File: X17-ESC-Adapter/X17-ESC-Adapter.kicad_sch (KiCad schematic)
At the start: 9 parts, among them J2 Power In/Out

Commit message: 10/12/24
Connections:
- net ESC2B: now also ESC5.5 (M2P2); no longer ESC5.6 (M2P3)
- net ESC2C: now also ESC5.6 (M2P3); no longer ESC5.5 (M2P2)

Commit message: before design review
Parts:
- added J1: Pad for ESC, Connector_Wire:SolderWirePad_1x01_SMD_1x2mm, symbol Connector:Conn_01x01_Pin
- J2: value Power In/Out -> PWM JST Connector
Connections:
- net +5V: now reaches BM08B-SRSS-TBLFSN1.1
- net +5V: now also J2.05
- net Current ADC: now reaches BM08B-SRSS-TBLFSN1.3
- net Current ADC: now also J2.07
- net Telemetry: now reaches BM08B-SRSS-TBLFSN1.4
- net Telemetry: now also J2.09
- net MTR_1 renamed PWM1
- net MTR_2 renamed PWM2
- net MTR_3 renamed PWM3
- net MTR_4 renamed PWM4
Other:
- moved on the sheet: ESC1, ESC2, ESC3, ESC4, ESC5

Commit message: made some changes
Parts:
- added J10, J11, J12, J13, J3, J4, J5, J6, J7, J8, J9: Pad for ESC, Custom ROV Parts:Pad for ESC Adapter, symbol Connector:Conn_01x01_Pin
- J1: footprint Connector_Wire:SolderWirePad_1x01_SMD_1x2mm -> Custom ROV Parts:Pad for ESC Adapter
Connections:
- net +5V: now also J2.09; no longer J2.05
- net ESC1A: now also ESC1.5, ESC1.6, J4.1 (Pin_1); no longer ESC1.1, ESC1.2
- net ESC1B: now also J3.1 (Pin_1)
- net ESC1C: now also ESC1.1, ESC1.2, J1.1 (Pin_1); no longer ESC1.5, ESC1.6
- net ESC2A: now also ESC2.5, ESC2.6, J7.1 (Pin_1); no longer ESC2.1, ESC2.2
- net ESC2B: now also J6.1 (Pin_1)
- net ESC2C: now also ESC2.1, ESC2.2, J5.1 (Pin_1); no longer ESC2.5, ESC2.6
- net ESC3A: now also J8.1 (Pin_1)
- net ESC3B: now also J10.1 (Pin_1)
- net ESC3C: now also J9.1 (Pin_1)
- net ESC4A: now also J11.1 (Pin_1)
- net ESC4B: now also J12.1 (Pin_1)
- net ESC4C: now also J13.1 (Pin_1)
- net PWM1: now also J2.10; no longer J2.04
- net PWM2: now also J2.08; no longer J2.06
- net PWM3: now also J2.06; no longer J2.08
- net PWM4: now also J2.04; no longer J2.10
- net Telemetry: now also J2.05; no longer J2.09
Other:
- note added: "Connection to Thrusters"
- note added: "Lumenier ESC"
- note added: "Power Testing LED"

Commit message: final before alumni design review
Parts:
- J1, J10, J11, J12, J13, J3, J4, J5, J6, J7, J8, J9: footprint Custom ROV Parts:Pad for ESC Adapter -> pad for esc connectors:Pad for ESC Adapter
- J2: value PWM JST Connector -> PWM Connector
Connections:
- net +12V: no longer J2.01
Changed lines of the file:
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@@
 	(wire
 		(pts
-			(xy 115.57 115.57) (xy 107.95 115.57)
-		)
-		(stroke
-			(width 0)
-			(type default)
-		)
-	)
-	(wire
-		(pts
 			(xy 135.89 95.25) (xy 143.51 95.25)
 		)
@@
 	(wire
 		(pts
-			(xy 81.28 96.52) (xy 81.28 92.71)
+			(xy 102.87 99.06) (xy 102.87 95.25)
 		)
 		(stroke
@@
 	(wire
 		(pts
-			(xy 67.31 96.52) (xy 67.31 92.71)
+			(xy 92.71 99.06) (xy 92.71 95.25)
 		)
 		(stroke
@@
 	(wire
 		(pts
-			(xy 97.79 96.52) (xy 97.79 92.71)
+			(xy 113.03 99.06) (xy 113.03 95.25)
 		)
 		(stroke
@@
 	(symbol
 		(lib_id "power:GND")
-		(at 81.28 96.52 0)
+		(at 102.87 99.06 0)
 		(unit 1)
 		(exclude_from_sim no)
@@
 		(fields_autoplaced yes)
 		(property "Reference" "#PWR012"
-			(at 81.28 102.87 0)
+			(at 102.87 105.41 0)
 			(effects
 				(font
@@
 		)
 		(property "Value" "GND"
-			(at 81.28 101.6 0)
+			(at 102.87 104.14 0)
 			(effects
 				(font
@@
 		)
 		(property "Footprint" ""
-			(at 81.28 96.52 0)
+			(at 102.87 99.06 0)
 			(effects
 				(font
@@
 		)
 		(property "Datasheet" ""
-			(at 81.28 96.52 0)
+			(at 102.87 99.06 0)
 			(effects
 				(font
@@
 		)
 		(property "Description" "Power symbol creates a global label with name \"GND\" , ground"
-			(at 81.28 96.52 0)
+			(at 102.87 99.06 0)
 			(effects
 				(font
@@
 	(symbol
 		(lib_id "power:PWR_FLAG")
-		(at 97.79 92.71 0)
+		(at 113.03 95.25 0)
 		(unit 1)
 		(exclude_from_sim no)
@@
 		(fields_autoplaced yes)
 		(property "Reference" "#FLG01"
-			(at 97.79 90.805 0)
+			(at 113.03 93.345 0)
 			(effects
 				(font
@@
 		)
 		(property "Value" "PWR_FLAG"
-			(at 97.79 87.63 0)
+			(at 113.03 90.17 0)
 			(effects
 				(font
@@
 		)
 		(property "Footprint" ""
-			(at 97.79 92.71 0)
+			(at 113.03 95.25 0)
 			(effects
 				(font
@@
 		)
 		(property "Datasheet" "~"
-			(at 97.79 92.71 0)
+			(at 113.03 95.25 0)
 			(effects
 				(font
@@
 		)
 		(property "Description" "Special symbol for telling ERC where power comes from"
-			(at 97.79 92.71 0)
+			(at 113.03 95.25 0)
 			(effects
 				(font
@@
 			)
 		)
-		(property "Footprint" "Custom ROV Parts:Pad for ESC Adapter"
+		(property "Footprint" "pad for esc connectors:Pad for ESC Adapter"
 			(at 219.71 102.87 0)
 			(effects
@@
 			)
 		)
-		(property "Footprint" "Custom ROV Parts:Pad for ESC Adapter"
+		(property "Footprint" "pad for esc connectors:Pad for ESC Adapter"
 			(at 220.98 111.76 0)
 			(effects
@@
 	(symbol
 		(lib_id "power:PWR_FLAG")
-		(at 67.31 92.71 0)
+		(at 92.71 95.25 0)
 		(unit 1)
 		(exclude_from_sim no)
@@
 		(fields_autoplaced yes)
 		(property "Reference" "#FLG03"
-			(at 67.31 90.805 0)
+			(at 92.71 93.345 0)
 			(effects
 				(font
@@
 		)
 		(property "Value" "PWR_FLAG"
-			(at 67.31 87.63 0)
+			(at 92.71 90.17 0)
 			(effects
 				(font
@@
 		)
 		(property "Footprint" ""
-			(at 67.31 92.71 0)
+			(at 92.71 95.25 0)
 			(effects
 				(font
@@
 		)
 		(property "Datasheet" "~"
-			(at 67.31 92.71 0)
+			(at 92.71 95.25 0)
 			(effects
 				(font
@@
 		)
 		(property "Description" "Special symbol for telling ERC where power comes from"
-			(at 67.31 92.71 0)
+			(at 92.71 95.25 0)
 			(effects
 				(font
@@
 	)
 	(symbol
-		(lib_id "power:+12V")
-		(at 107.95 115.57 90)
-		(unit 1)
-		(exclude_from_sim no)
-		(in_bom yes)
-		(on_board yes)
-		(dnp no)
-		(fields_autoplaced yes)
-		(property "Reference" "#PWR03"
-			(at 111.76 115.57 0)
-			(effects
-				(font
-					(size 1.27 1.27)
-				)
-				(hide yes)
-			)
-		)
-		(property "Value" "+12V"
-			(at 104.14 115.5699 90)
-			(effects
-				(font
-					(size 1.27 1.27)
-				)
-				(justify left)
-			)
-		)
-		(property "Footprint" ""
-			(at 107.95 115.57 0)
-			(effects
-				(font
-					(size 1.27 1.27)
-				)
-				(hide yes)
-			)
-		)
-		(property "Datasheet" ""
-			(at 107.95 115.57 0)
-			(effects
-				(font
-					(size 1.27 1.27)
-				)
-				(hide yes)
-			)
-		)
-		(property "Description" "Power symbol creates a global label with name \"+12V\""
-			(at 107.95 115.57 0)
-			(effects
-				(font
-					(size 1.27 1.27)
-				)
-				(hide yes)
-			)
-		)
-		(pin "1"
-		)
-		(instances
-			(project ""
-				(path "/4ecb7723-5f96-464b-bb69-f7f22417a45a"
-					(reference "#PWR03")
-					(unit 1)
-				)
-			)
-		)
-	)
-	(symbol
 		(lib_id "CONN_1824750000_WED:1824750000")
 		(at 179.07 118.11 0)
@@
 			)
 		)
-		(property "Footprint" "Custom ROV Parts:Pad for ESC Adapter"
+		(property "Footprint" "pad for esc connectors:Pad for ESC Adapter"
 			(at 219.71 95.25 0)
 			(effects
@@
 			)
 		)
-		(property "Value" "PWM JST Connector"
+		(property "Value" "PWM Connector"
 			(at 128.27 110.49 0)
 			(effects
@@
 			)
 		)
-		(property "Footprint" "Custom ROV Parts:Pad for ESC Adapter"
+		(property "Footprint" "pad for esc connectors:Pad for ESC Adapter"
 			(at 219.71 87.63 0)
 			(effects
@@
 			)
 		)
-		(property "Footprint" "Custom ROV Parts:Pad for ESC Adapter"
+		(property "Footprint" "pad for esc connectors:Pad for ESC Adapter"
 			(at 175.26 95.25 0)
 			(effects
@@
 			)
 		)
-		(property "Footprint" "Custom ROV Parts:Pad for ESC Adapter"
+		(property "Footprint" "pad for esc connectors:Pad for ESC Adapter"
 			(at 175.26 102.87 0)
 			(effects
@@
 	(symbol
 		(lib_id "power:+12V")
-		(at 97.79 96.52 180)
+		(at 113.03 99.06 180)
 		(unit 1)
 		(exclude_from_sim no)
@@
 		(fields_autoplaced yes)
 		(property "Reference" "#PWR011"
-			(at 97.79 92.71 0)
+			(at 113.03 95.25 0)
 			(effects
 				(font
@@
 		)
 		(property "Value" "+12V"
-			(at 97.79 101.6 0)
+			(at 113.03 104.14 0)
 			(effects
 				(font
@@
 		)
 		(property "Footprint" ""
-			(at 97.79 96.52 0)
+			(at 113.03 99.06 0)
 			(effects
 				(font
@@
 		)
 		(property "Datasheet" ""
-			(at 97.79 96.52 0)
+			(at 113.03 99.06 0)
 			(effects
 				(font
@@
 		)
 		(property "Description" "Power symbol creates a global label with name \"+12V\""
-			(at 97.79 96.52 0)
+			(at 113.03 99.06 0)
 			(effects
 				(font
@@
 			)
 		)
-		(property "Footprint" "Custom ROV Parts:Pad for ESC Adapter"
+		(property "Footprint" "pad for esc connectors:Pad for ESC Adapter"
 			(at 175.26 119.38 0)
 			(effects
@@
 			)
 		)
-		(property "Footprint" "Custom ROV Parts:Pad for ESC Adapter"
+		(property "Footprint" "pad for esc connectors:Pad for ESC Adapter"
 			(at 220.98 119.38 0)
 			(effects
@@
 	(symbol
 		(lib_id "power:PWR_FLAG")
-		(at 81.28 92.71 0)
+		(at 102.87 95.25 0)
 		(unit 1)
 		(exclude_from_sim no)
@@
 		(fields_autoplaced yes)
 		(property "Reference" "#FLG02"
-			(at 81.28 90.805 0)
+			(at 102.87 93.345 0)
 			(effects
 				(font
@@
 		)
 		(property "Value" "PWR_FLAG"
-			(at 81.28 87.63 0)
+			(at 102.87 90.17 0)
 			(effects
 				(font
@@
 		)
 		(property "Footprint" ""
-			(at 81.28 92.71 0)
+			(at 102.87 95.25 0)
 			(effects
 				(font
@@
 		)
 		(property "Datasheet" "~"
-			(at 81.28 92.71 0)
+			(at 102.87 95.25 0)
 			(effects
 				(font
@@
 		)
 		(property "Description" "Special symbol for telling ERC where power comes from"
-			(at 81.28 92.71 0)
+			(at 102.87 95.25 0)
 			(effects
 				(font
@@
 			)
 		)
-		(property "Footprint" "Custom ROV Parts:Pad for ESC Adapter"
+		(property "Footprint" "pad for esc connectors:Pad for ESC Adapter"
 			(at 175.26 87.63 0)
 			(effects
@@
 	(symbol
 		(lib_id "power:+5V")
-		(at 67.31 96.52 180)
+		(at 92.71 99.06 180)
 		(unit 1)
 		(exclude_from_sim no)
@@
 		(fields_autoplaced yes)
 		(property "Reference" "#PWR013"
-			(at 67.31 92.71 0)
+			(at 92.71 95.25 0)
 			(effects
 				(font
@@
 		)
 		(property "Value" "+5V"
-			(at 67.31 101.6 0)
+			(at 92.71 104.14 0)
 			(effects
 				(font
@@
 		)
 		(property "Footprint" ""
-			(at 67.31 96.52 0)
+			(at 92.71 99.06 0)
 			(effects
 				(font
@@
 		)
 		(property "Datasheet" ""
-			(at 67.31 96.52 0)
+			(at 92.71 99.06 0)
 			(effects
 				(font
@@
 		)
 		(property "Description" "Power symbol creates a global label with name \"+5V\""
-			(at 67.31 96.52 0)
+			(at 92.71 99.06 0)
 			(effects
 				(font
@@
 			)
 		)
-		(property "Footprint" "Custom ROV Parts:Pad for ESC Adapter"
+		(property "Footprint" "pad for esc connectors:Pad for ESC Adapter"
 			(at 220.98 127 0)
 			(effects
@@
 			)
 		)
-		(property "Footprint" "Custom ROV Parts:Pad for ESC Adapter"
+		(property "Footprint" "pad for esc connectors:Pad for ESC Adapter"
 			(at 175.26 111.76 0)
 			(effects
@@
 			)
 		)
-		(property "Footprint" "Custom ROV Parts:Pad for ESC Adapter"
+		(property "Footprint" "pad for esc connectors:Pad for ESC Adapter"
 			(at 175.26 127 0)
 			(effects

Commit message: yeet
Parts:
- R2: value 470 Ω -> 1K Ω
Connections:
- net +12V: now also J2.01
- net +5V: now also J2.05; no longer J2.09
- net PWM1: now also J2.04; no longer J2.10
- net PWM2: now also J2.06; no longer J2.08
- net PWM3: now also J2.08; no longer J2.06
- net PWM4: now also J2.10; no longer J2.04
- net Telemetry: now also J2.09; no longer J2.05

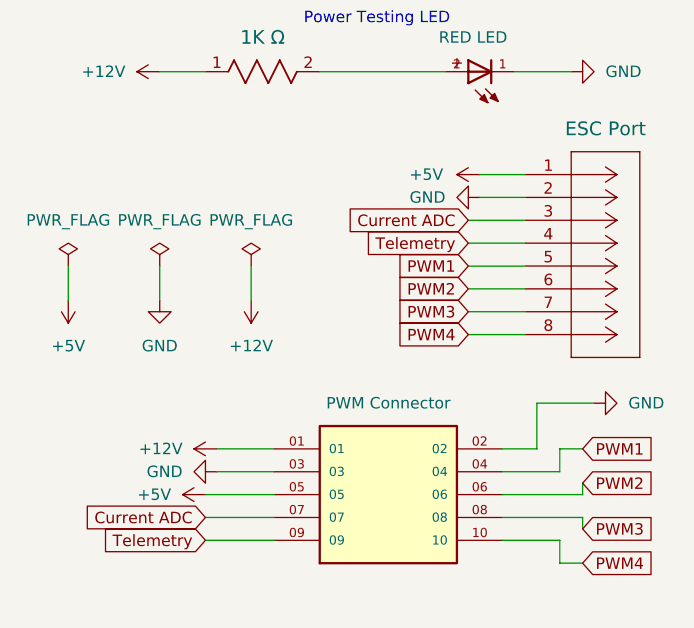
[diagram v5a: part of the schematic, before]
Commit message: daniel edit for correct pwm header position + polygon adjustment
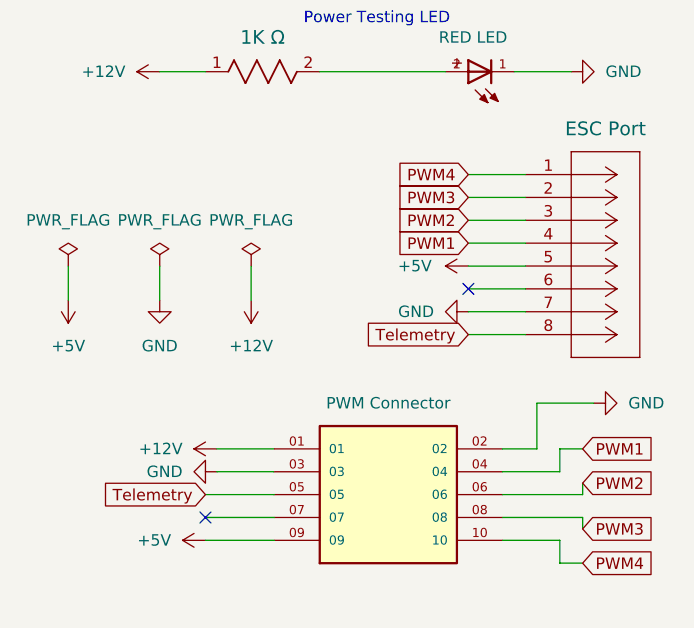
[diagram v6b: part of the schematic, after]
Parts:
- BM08B-SRSS-TBLFSN1: footprint CONN_BM08B-SRSS-TBLFSN_JST -> Custom:CONN_BM08B-SRSS-TBLFSN_JST
- D1: footprint led:WL-SMCW_0805 -> Diode_SMD:D_0805_2012Metric
- J2: footprint IPS1-105-01-L-D:SAMTEC_IPS1-105-01-L-D -> Custom:PWM, 12V, GND JST Connector
- R2: footprint STA_RMCF0603_STP -> Resistor_SMD:R_0603_1608Metric
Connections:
- net +5V: now also BM08B-SRSS-TBLFSN1.5, J2.09; no longer BM08B-SRSS-TBLFSN1.1, J2.05
- net GND: now also BM08B-SRSS-TBLFSN1.7; no longer BM08B-SRSS-TBLFSN1.2
- net PWM1: now also BM08B-SRSS-TBLFSN1.4; no longer BM08B-SRSS-TBLFSN1.5
- net PWM2: now also BM08B-SRSS-TBLFSN1.3; no longer BM08B-SRSS-TBLFSN1.6
- net PWM3: now also BM08B-SRSS-TBLFSN1.2; no longer BM08B-SRSS-TBLFSN1.7
- net PWM4: now also BM08B-SRSS-TBLFSN1.1; no longer BM08B-SRSS-TBLFSN1.8
- net Telemetry: now also BM08B-SRSS-TBLFSN1.8, J2.05; no longer BM08B-SRSS-TBLFSN1.4, J2.09
- net Current ADC: no longer names the net of J2.07
- net Current ADC: no longer BM08B-SRSS-TBLFSN1.3
- no-connect marks 0 -> 2

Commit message: changes 1/3/25
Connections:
- net +5V: now also BM08B-SRSS-TBLFSN1.8; no longer BM08B-SRSS-TBLFSN1.5
- net Telemetry: now also BM08B-SRSS-TBLFSN1.5; no longer BM08B-SRSS-TBLFSN1.8
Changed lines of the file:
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@@
+		)
+	)
+	(global_label "PWM2"
+		(shape input)
+		(at 149.86 119.38 0)
+		(fields_autoplaced yes)
+		(effects
+			(font
+				(size 1.27 1.27)
+			)
+			(justify left)
+		)
+		(property "Intersheetrefs" "${INTERSHEET_REFS}"
+			(at 158.2275 119.38 0)
+			(effects
+				(font
+					(size 1.27 1.27)
+				)
+				(justify left)
+				(hide yes)
+			)
+		)
+	)
+	(global_label "ESC3B"
+		(shape input)
+		(at 173.99 124.46 180)
+		(fields_autoplaced yes)
+		(effects
+			(font
+				(size 1.27 1.27)
+			)
+			(justify right)
+		)
+		(property "Intersheetrefs" "${INTERSHEET_REFS}"
+			(at 164.8968 124.46 0)
+			(effects
+				(font
+					(size 1.27 1.27)
+				)
+				(justify right)
+				(hide yes)
+			)
+		)
+	)
+	(global_label "ESC1B"
+		(shape input)
+		(at 173.99 100.33 180)
+		(fields_autoplaced yes)
+		(effects
+			(font
+				(size 1.27 1.27)
+			)
+			(justify right)
+		)
+		(property "Intersheetrefs" "${INTERSHEET_REFS}"
+			(at 164.8968 100.33 0)
+			(effects
+				(font
+					(size 1.27 1.27)
+				)
+				(justify right)
+				(hide yes)
+			)
+		)
+	)
+	(global_label "ESC1C"
+		(shape input)
+		(at 173.99 92.71 180)
+		(fields_autoplaced yes)
+		(effects
+			(font
+				(size 1.27 1.27)
+			)
+			(justify right)
+		)
+		(property "Intersheetrefs" "${INTERSHEET_REFS}"
+			(at 164.8968 92.71 0)
+			(effects
+				(font
+					(size 1.27 1.27)
+				)
+				(justify right)
+				(hide yes)
+			)
+		)
+	)
+	(global_label "ESC3B"
+		(shape input)
+		(at 220.98 53.34 0)
+		(fields_autoplaced yes)
+		(effects
+			(font
+				(size 1.27 1.27)
+			)
+			(justify left)
+		)
+		(property "Intersheetrefs" "${INTERSHEET_REFS}"
+			(at 230.0732 53.34 0)
+			(effects
+				(font
+					(size 1.27 1.27)
+				)
+				(justify left)
+				(hide yes)
+			)
 		)
 	)
 	(global_label "Telemetry"
 		(shape input)
-		(at 137.16 102.87 180)
+		(at 137.16 95.25 180)
 		(fields_autoplaced yes)
 		(effects
@@
 		)
 		(property "Intersheetrefs" "${INTERSHEET_REFS}"
-			(at 125.1034 102.87 0)
+			(at 125.1034 95.25 0)
 			(effects
 				(font
@@
 				)
 				(justify right)
-				(hide yes)
-			)
-		)
-	)
-	(global_label "PWM2"
-		(shape input)
-		(at 149.86 119.38 0)
-		(fields_autoplaced yes)
-		(effects
-			(font
-				(size 1.27 1.27)
-			)
-			(justify left)
-		)
-		(property "Intersheetrefs" "${INTERSHEET_REFS}"
-			(at 158.2275 119.38 0)
-			(effects
-				(font
-					(size 1.27 1.27)
-				)
-				(justify left)
-				(hide yes)
-			)
-		)
-	)
-	(global_label "ESC3B"
-		(shape input)
-		(at 173.99 124.46 180)
-		(fields_autoplaced yes)
-		(effects
-			(font
-				(size 1.27 1.27)
-			)
-			(justify right)
-		)
-		(property "Intersheetrefs" "${INTERSHEET_REFS}"
-			(at 164.8968 124.46 0)
-			(effects
-				(font
-					(size 1.27 1.27)
-				)
-				(justify right)
-				(hide yes)
-			)
-		)
-	)
-	(global_label "ESC1B"
-		(shape input)
-		(at 173.99 100.33 180)
-		(fields_autoplaced yes)
-		(effects
-			(font
-				(size 1.27 1.27)
-			)
-			(justify right)
-		)
-		(property "Intersheetrefs" "${INTERSHEET_REFS}"
-			(at 164.8968 100.33 0)
-			(effects
-				(font
-					(size 1.27 1.27)
-				)
-				(justify right)
-				(hide yes)
-			)
-		)
-	)
-	(global_label "ESC1C"
-		(shape input)
-		(at 173.99 92.71 180)
-		(fields_autoplaced yes)
-		(effects
-			(font
-				(size 1.27 1.27)
-			)
-			(justify right)
-		)
-		(property "Intersheetrefs" "${INTERSHEET_REFS}"
-			(at 164.8968 92.71 0)
-			(effects
-				(font
-					(size 1.27 1.27)
-				)
-				(justify right)
-				(hide yes)
-			)
-		)
-	)
-	(global_label "ESC3B"
-		(shape input)
-		(at 220.98 53.34 0)
-		(fields_autoplaced yes)
-		(effects
-			(font
-				(size 1.27 1.27)
-			)
-			(justify left)
-		)
-		(property "Intersheetrefs" "${INTERSHEET_REFS}"
-			(at 230.0732 53.34 0)
-			(effects
-				(font
-					(size 1.27 1.27)
-				)
-				(justify left)
 				(hide yes)
 			)
@@
 				(path "/4ecb7723-5f96-464b-bb69-f7f22417a45a"
 					(reference "J11")
+					(unit 1)
+				)
+			)
+		)
+	)
+	(symbol
+		(lib_id "power:+5V")
+		(at 137.16 102.87 90)
+		(unit 1)
+		(exclude_from_sim no)
+		(in_bom yes)
+		(on_board yes)
+		(dnp no)
+		(property "Reference" "#PWR014"
+			(at 140.97 102.87 0)
+			(effects
+				(font
+					(size 1.27 1.27)
+				)
+				(hide yes)
+			)
+		)
+		(property "Value" "+5V"
+			(at 133.096 102.87 90)
+			(effects
+				(font
+					(size 1.27 1.27)
+				)
+				(justify left)
+			)
+		)
+		(property "Footprint" ""
+			(at 137.16 102.87 0)
+			(effects
+				(font
+					(size 1.27 1.27)
+				)
+				(hide yes)
+			)
+		)
+		(property "Datasheet" ""
+			(at 137.16 102.87 0)
+			(effects
+				(font
+					(size 1.27 1.27)
+				)
+				(hide yes)
+			)
+		)
+		(property "Description" "Power symbol creates a global label with name \"+5V\""
+			(at 137.16 102.87 0)
+			(effects
+				(font
+					(size 1.27 1.27)
+				)
+				(hide yes)
+			)
+		)
+		(pin "1"
+		)
+		(instances
+			(project "X17-ESC-Adapter"
+				(path "/4ecb7723-5f96-464b-bb69-f7f22417a45a"
+					(reference "#PWR014")
 					(unit 1)
 				)
@@
 					(unit 1)
 				)
-			)
-		)
-	)
-	(symbol
-		(lib_id "power:+5V")
-		(at 137.16 95.25 90)
-		(unit 1)
-		(exclude_from_sim no)
-		(in_bom yes)
-		(on_board yes)
-		(dnp no)
-		(property "Reference" "#PWR09"
-			(at 140.97 95.25 0)
-			(effects
-				(font
-					(size 1.27 1.27)
-				)
-				(hide yes)
-			)
-		)
-		(property "Value" "+5V"
-			(at 133.096 95.25 90)
-			(effects
-				(font
-					(size 1.27 1.27)
-				)
-				(justify left)
-			)
-		)
-		(property "Footprint" ""
-			(at 137.16 95.25 0)
-			(effects
-				(font
-					(size 1.27 1.27)
-				)
-				(hide yes)
-			)
-		)
-		(property "Datasheet" ""
-			(at 137.16 95.25 0)
-			(effects
-				(font
-					(size 1.27 1.27)
-				)
-				(hide yes)
-			)
-		)
-		(property "Description" "Power symbol creates a global label with name \"+5V\""
-			(at 137.16 95.25 0)
-			(effects
-				(font
-					(size 1.27 1.27)
-				)
-				(hide yes)
-			)
-		)
-		(pin "1"
-		)
-		(instances
-			(project ""
-				(path "/4ecb7723-5f96-464b-bb69-f7f22417a45a"
-					(reference "#PWR09")
-					(unit 1)
-				)
